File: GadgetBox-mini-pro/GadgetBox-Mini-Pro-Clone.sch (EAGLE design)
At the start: 25 parts, among them U1 MCP73831T-2ACI/OT, U2 AP2112-3.3

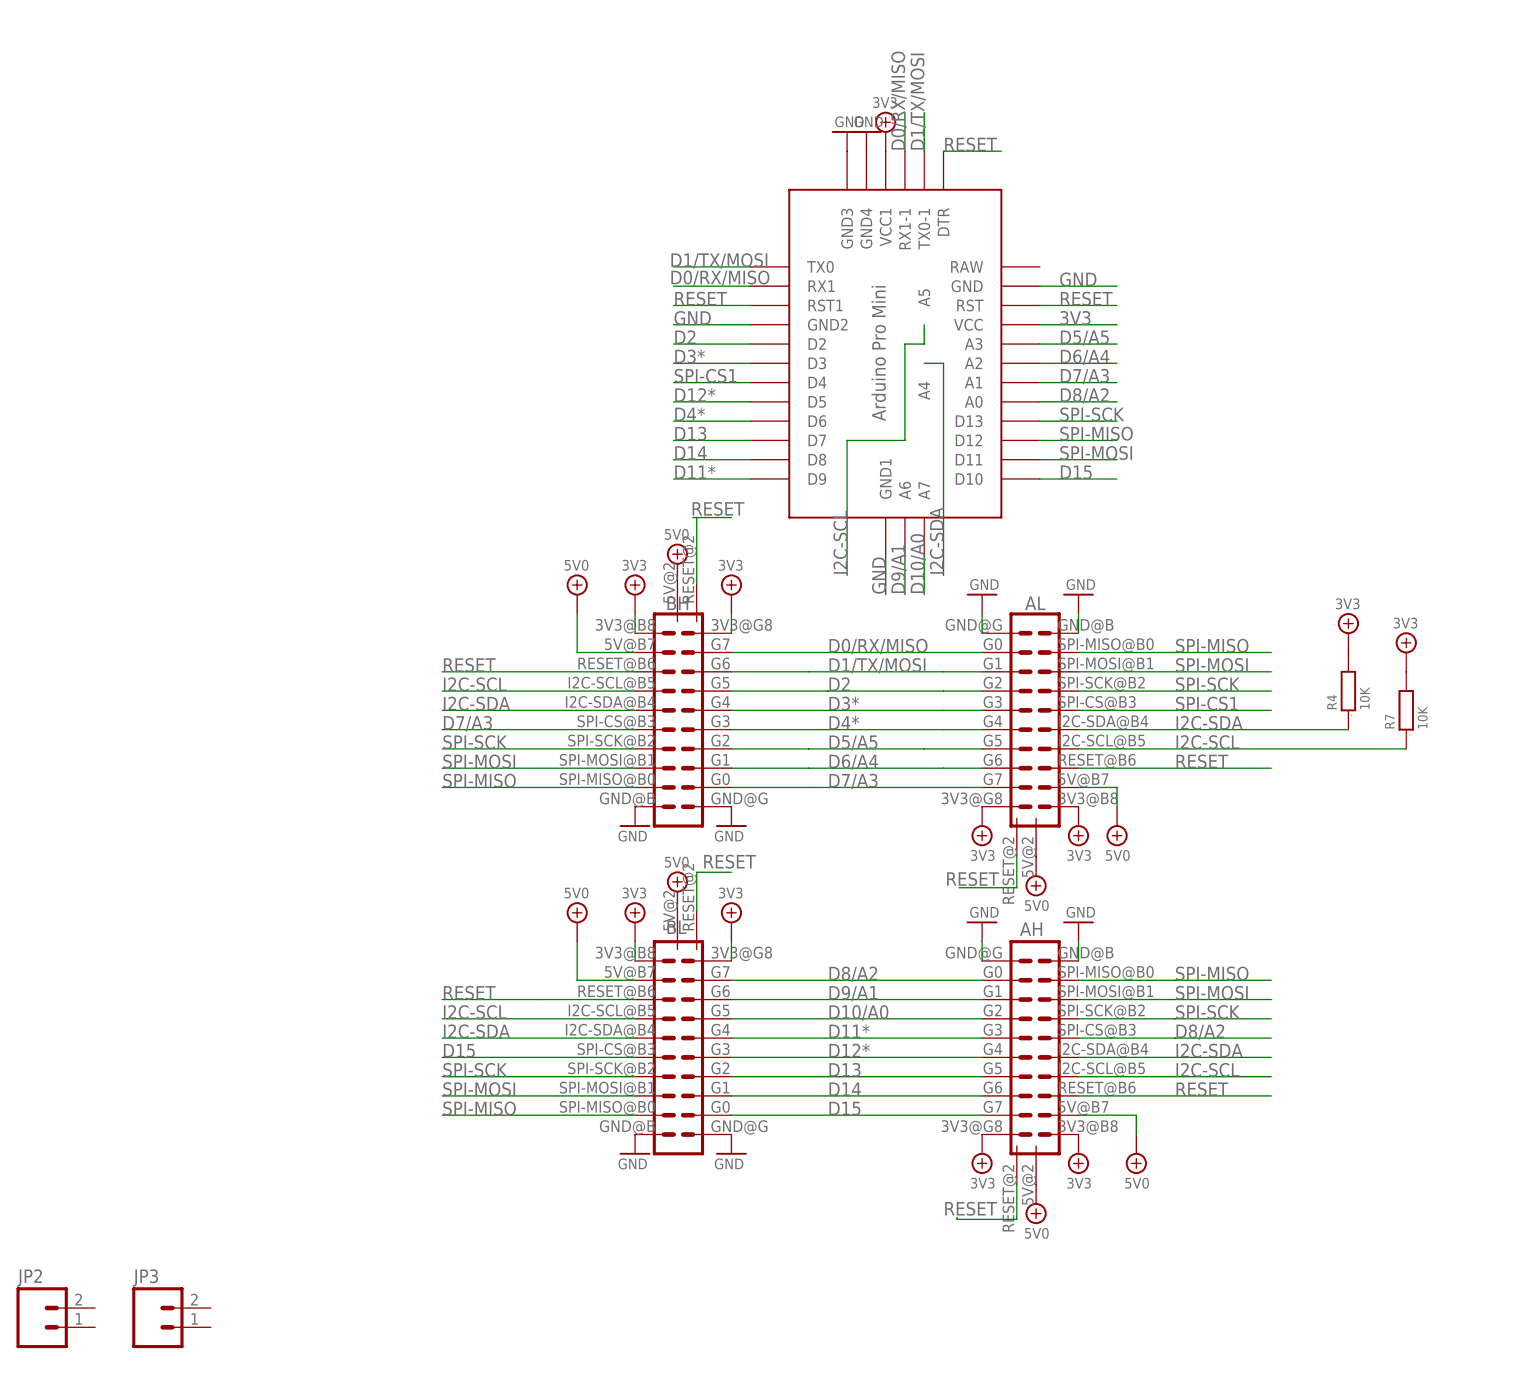
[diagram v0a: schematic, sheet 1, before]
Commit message: Redid the Mini Pro Clone with better routing.
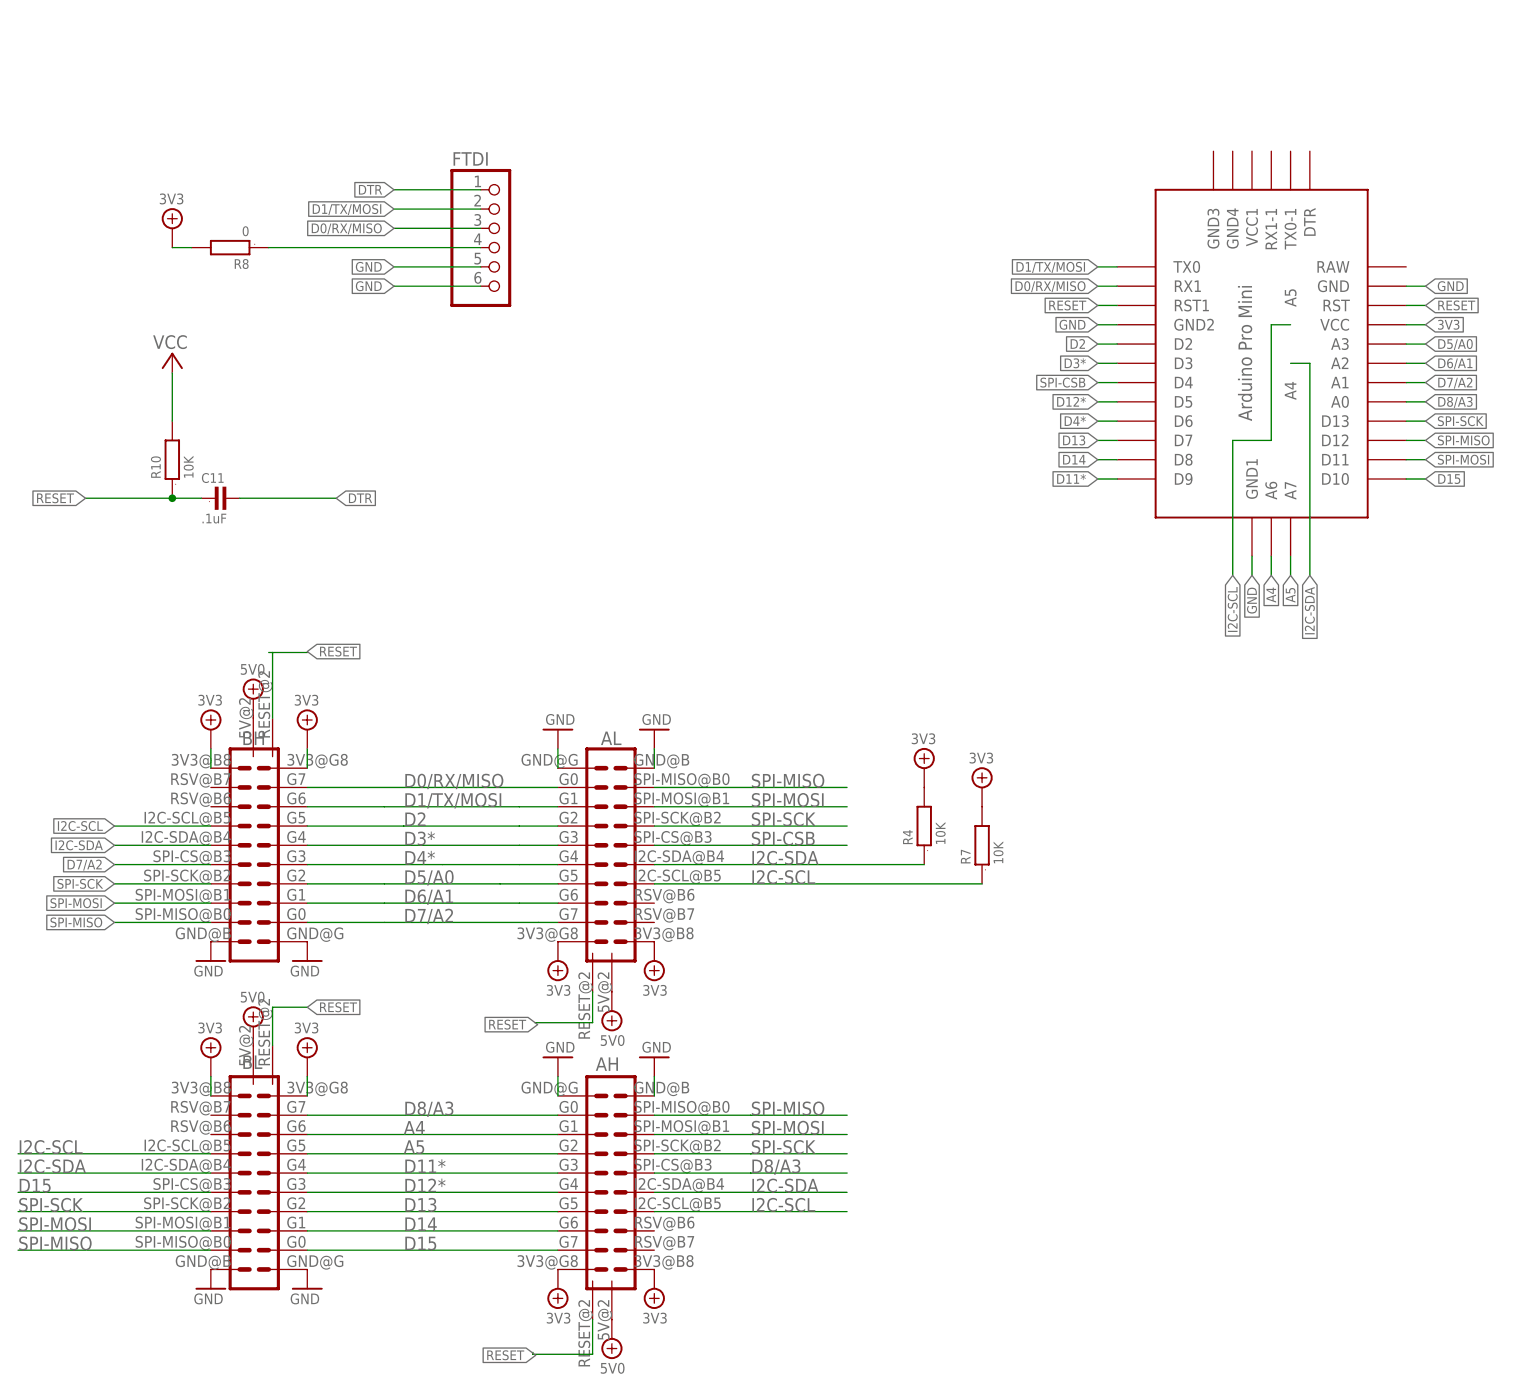
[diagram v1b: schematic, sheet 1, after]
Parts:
- removed JP2, JP3: (no value), SparkFun:M021X02_NO_SILK
- added C11: .1uF, GadgetFactory:C0805
- added FTDI: (no value), GadgetFactory:PINHD-1X6
- added R10: 10K, GadgetFactory:R0603
- added R8: 0, GadgetFactory:R0603
- JP1: PARTNO B2B-PH-SM4-TB(LF)(SN),JST SALES AMERICA INC (VA),dk,455-1734-1-ND ,"2 Positions Header, Shrouded Connector 0.079"" (2.00mm) Through Hole Tin ", REF87 -> B2B-PH-SM4-TB(LF)(SN),JST SALES AMERICA INC (VA),dk,455-1734-1-ND ,"2 Positions Header, Shrouded Connector 0.079 (2.00mm) Through Hole Tin ", REF87
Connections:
- net D10/A0 renamed A5
- net D5/A5 renamed D5/A0
- net D6/A4 renamed D6/A1
- net D7/A3 renamed D7/A2
- net D8/A2 renamed D8/A3
- net D9/A1 renamed A4
- net SPI-CS1 renamed SPI-CSB
- new net DTR: C11.2, FTDI.1
- new net N$5: FTDI.4, R8A.1
- net 3V3: now also R10A.2, R8A.2; no longer U$1.VCC1
- net 5V0: no longer AH.5V@B7, AL.5V@B7, BH.5V@B7, BL.5V@B7
- net D0/RX/MISO: now also FTDI.3; no longer U$1.RX1-1
- net D1/TX/MOSI: now also FTDI.2; no longer U$1.TX0-1
- net GND: now also FTDI.5, FTDI.6; no longer U$1.GND3, U$1.GND4
- net RESET: now also C11.1, R10A.1; no longer AH.RESET@B6, AL.RESET@B6, BH.RESET@B6, BL.RESET@B6, U$1.DTR
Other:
- moved on the sheet: AH, AL, BH, BL, R4, R7
